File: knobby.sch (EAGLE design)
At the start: 15 parts

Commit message: Added LEDS to knobby board
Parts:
- added P1, P101: (no value), DCO_PIGGY:SPARKFUN_POTPDB12
- added S3: SWITCH-MOMENTARY-2-SMD-1101NE, SparkFun-Electromechanical:SWITCH-MOMENTARY-2-SMD-1101NE
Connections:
- net 5V: now also P1.E, P101.E
- net CLOCK_SPEED: now also P101.S
- net GND: now also S3.2
- net LOAD: now also S3.1
- net NOTE_LENGTH: now also P1.S
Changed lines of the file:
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@@
 <layer number="108" name="tplace-old" color="10" fill="1" visible="yes" active="yes"/>
 <layer number="109" name="ref-old" color="11" fill="1" visible="yes" active="yes"/>
+<layer number="110" name="fp0" color="7" fill="1" visible="yes" active="yes"/>
+<layer number="111" name="LPC17xx" color="7" fill="1" visible="yes" active="yes"/>
 <layer number="116" name="Patch_BOT" color="9" fill="4" visible="no" active="yes"/>
 <layer number="121" name="_tsilk" color="7" fill="1" visible="no" active="yes"/>
 <layer number="122" name="_bsilk" color="7" fill="1" visible="no" active="yes"/>
+<layer number="123" name="tTestmark" color="7" fill="1" visible="yes" active="yes"/>
+<layer number="124" name="bTestmark" color="7" fill="1" visible="yes" active="yes"/>
 <layer number="125" name="_tNames" color="7" fill="1" visible="no" active="yes"/>
+<layer number="131" name="tAdjust" color="7" fill="1" visible="yes" active="yes"/>
+<layer number="132" name="bAdjust" color="7" fill="1" visible="yes" active="yes"/>
 <layer number="144" name="Drill_legend" color="7" fill="1" visible="no" active="yes"/>
 <layer number="151" name="HeatSink" color="7" fill="1" visible="no" active="yes"/>
@@
 <part name="S1" library="SparkFun-Electromechanical" deviceset="SWITCH-MOMENTARY-2" device="-SMD-1101NE"/>
 <part name="S2" library="SparkFun-Electromechanical" deviceset="SWITCH-MOMENTARY-2" device="-SMD-1101NE"/>
+<part name="P101" library="DCO_PIGGY" deviceset="SPARKFUN_POT" device="PDB12"/>
+<part name="SUPPLY2" library="SparkFun-Aesthetics" deviceset="5V" device=""/>
+<part name="P1" library="DCO_PIGGY" deviceset="SPARKFUN_POT" device="PDB12"/>
+<part name="SUPPLY3" library="SparkFun-Aesthetics" deviceset="5V" device=""/>
+<part name="S3" library="SparkFun-Electromechanical" deviceset="SWITCH-MOMENTARY-2" device="-SMD-1101NE"/>
+<part name="GND2" library="SparkFun-Aesthetics" deviceset="GND" device=""/>
 </parts>
 <sheets>
@@
 <instance part="S1" gate="G$1" x="-172.72" y="96.52"/>
 <instance part="S2" gate="G$1" x="-172.72" y="96.52"/>
+<instance part="P101" gate="G$1" x="-170.18" y="83.82" rot="R270"/>
+<instance part="SUPPLY2" gate="G$1" x="-162.56" y="86.36"/>
+<instance part="P1" gate="G$1" x="-172.72" y="68.58" rot="R270"/>
+<instance part="SUPPLY3" gate="G$1" x="-165.1" y="71.12"/>
+<instance part="S3" gate="G$1" x="-175.26" y="50.8"/>
+<instance part="GND2" gate="1" x="-170.18" y="45.72"/>
 </instances>
 <busses>
@@
 <wire x1="-139.7" y1="165.1" x2="-139.7" y2="167.64" width="0.1524" layer="91"/>
 </segment>
+<segment>
+<pinref part="P101" gate="G$1" pin="E"/>
+<wire x1="-162.56" y1="83.82" x2="-162.56" y2="86.36" width="0.1524" layer="91"/>
+<pinref part="SUPPLY2" gate="G$1" pin="5V"/>
+</segment>
+<segment>
+<pinref part="P1" gate="G$1" pin="E"/>
+<pinref part="SUPPLY3" gate="G$1" pin="5V"/>
+<wire x1="-165.1" y1="68.58" x2="-165.1" y2="71.12" width="0.1524" layer="91"/>
+</segment>
 </net>
 <net name="GND" class="0">
@@
 <pinref part="GND1" gate="1" pin="GND"/>
 </segment>
+<segment>
+<pinref part="S3" gate="G$1" pin="2"/>
+<pinref part="GND2" gate="1" pin="GND"/>
+<wire x1="-170.18" y1="50.8" x2="-170.18" y2="48.26" width="0.1524" layer="91"/>
+</segment>
 </net>
 <net name="PAUSE_IN" class="0">
@@
 <pinref part="JP3" gate="G$1" pin="17"/>
 <wire x1="-148.59" y1="157.48" x2="-146.05" y2="157.48" width="0.1524" layer="91"/>
+</segment>
+<segment>
+<pinref part="S3" gate="G$1" pin="1"/>
+<wire x1="-180.34" y1="50.8" x2="-185.42" y2="50.8" width="0.1524" layer="91"/>
+<label x="-187.96" y="50.8" size="1.778" layer="95"/>
 </segment>
 </net>
@@
 <label x="-177.8" y="157.48" size="1.778" layer="95"/>
 </segment>
+<segment>
+<pinref part="P101" gate="G$1" pin="S"/>
+<wire x1="-170.18" y1="78.74" x2="-170.18" y2="76.2" width="0.1524" layer="91"/>
+<wire x1="-170.18" y1="76.2" x2="-185.42" y2="76.2" width="0.1524" layer="91"/>
+<label x="-187.96" y="76.2" size="1.778" layer="95"/>
+</segment>
 </net>
 <net name="N$29" class="0">
@@
 <label x="-147.32" y="160.02" size="1.778" layer="95"/>
 </segment>
-</net>
+<segment>
+<pinref part="P1" gate="G$1" pin="S"/>
+<wire x1="-172.72" y1="63.5" x2="-172.72" y2="60.96" width="0.1524" layer="91"/>
+<wire x1="-172.72" y1="60.96" x2="-187.96" y2="60.96" width="0.1524" layer="91"/>
+<label x="-190.5" y="60.96" size="1.778" layer="95"/>
+</segment>
+</net>

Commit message: 16 pots
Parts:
- added LED1, LED10, LED11, LED12, LED13, LED14, LED15, LED16, LED2, LED3, LED4, LED5, LED6, LED7, LED8, LED9: (no value), SparkFun-LED:LED0603
- added P10, P11, P12, P13, P14, P15, P16, P17, P2, P3, P4, P5, P6, P7, P8, P9: 10k, DCO_PIGGY:SPARKFUN_POTPDB12
- added R1, R13, R14, R15, R16, R17, R18, R19, R2, R20, R21, R22, R23, R24, R3, R4: 15k, SparkFun-Resistors:RESISTOR0603
- added S10, S11, S12, S13, S14, S15, S16, S17, S18, S19, S4, S5, S6, S7, S8, S9: SWITCH-MOMENTARY-2-SMD-1101NE, SparkFun-Electromechanical:SWITCH-MOMENTARY-2-SMD-1101NE
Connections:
- new net CHANNEL3: P5.S
- new net N$1: P2.E, R1.1
- new net N$10: P6.A, S8.2
- new net N$11: P7.E, R14.1
- new net N$12: P7.A, S9.2
- new net N$13: P8.E, R15.1
- new net N$14: P8.A, S10.2
- new net N$15: P9.E, R16.1
- new net N$16: P9.A, S11.2
- new net N$17: P10.E, R17.1
- new net N$18: P10.A, S12.2
- new net N$19: P11.E, R18.1
- new net N$2: P2.A, S4.2
- new net N$20: P11.A, S13.2
- new net N$21: P12.E, R19.1
- new net N$22: P12.A, S14.2
- new net N$23: P13.E, R20.1
- new net N$24: P13.A, S15.2
- new net N$25: P14.E, R21.1
- new net N$26: P14.A, S16.2
- new net N$27: P15.E, R22.1
- new net N$28: P15.A, S17.2
- new net N$3: P3.E, R2.1
- new net N$30: P16.E, R23.1
- new net N$31: P16.A, S18.2
- new net N$32: P17.E, R24.1
- new net N$33: P17.A, S19.2
- new net N$4: P3.A, S5.2
- new net N$5: P4.E, R3.1
- new net N$6: P4.A, S6.2
- new net N$7: P5.E, R4.1
- new net N$8: P5.A, S7.2
- new net N$9: P6.E, R13.1
- net 5V: now also R1.2, R13.2, R14.2, R15.2, R16.2, R17.2, R18.2, R19.2, R2.2, R20.2, R21.2, R22.2, R23.2, R24.2, R3.2, R4.2
- net CHANNEL0: now also P2.S
- net CHANNEL1: now also P3.S
- net CHANNEL10: now also P10.S
- net CHANNEL11: now also P11.S
- net CHANNEL12: now also P12.S
- net CHANNEL13: now also P13.S
- net CHANNEL14: now also P16.S
- net CHANNEL15: now also P17.S
- net CHANNEL2: now also P4.S
- net CHANNEL4: now also P6.S
- net CHANNEL5: now also P7.S
- net CHANNEL6: now also P14.S
- net CHANNEL7: now also P15.S
- net CHANNEL8: now also P8.S
- net CHANNEL9: now also P9.S
- net GND: now also LED1.C, LED10.C, LED11.C, LED12.C, LED13.C, LED14.C, LED15.C, LED16.C, LED2.C, LED3.C, LED4.C, LED5.C, LED6.C, LED7.C, LED8.C, LED9.C, S10.1, S11.1, S12.1, S13.1, S14.1, S15.1, S16.1, S17.1, S18.1, S19.1, S4.1, S5.1, S6.1, S7.1, S8.1, S9.1
- net LED0: now also LED16.A
- net LED1: now also LED7.A
- net LED10: now also LED11.A
- net LED11: now also LED12.A
- net LED12: now also LED13.A
- net LED13: now also LED14.A
- net LED14: now also LED15.A
- net LED15: now also LED1.A
- net LED2: now also LED6.A
- net LED3: now also LED5.A
- net LED4: now also LED4.A
- net LED5: now also LED3.A
- net LED6: now also LED2.A
- net LED7: now also LED8.A
- net LED8: now also LED9.A
- net LED9: now also LED10.A

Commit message: knobby brd
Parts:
- removed FRAME1: FRAME-LETTER, SparkFun-Aesthetics:FRAME-LETTER
- removed JP2, JP3: M20, SparkFun-Connectors:M20
- removed LED1, LED10, LED11, LED12, LED13, LED14, LED15, LED16, LED2, LED3, LED4, LED5, LED6, LED7, LED8, LED9: (no value), SparkFun-LED:LED0603
- removed P1, P101: (no value), DCO_PIGGY:SPARKFUN_POTPDB12
- removed P10, P11, P12, P13, P14, P15, P16, P17, P2, P3, P4, P5, P6, P7, P8, P9: 10k, DCO_PIGGY:SPARKFUN_POTPDB12
- removed R13, R14, R15, R16, R17, R18, R19, R2, R20, R21, R22, R23, R24, R3, R4: 15k, SparkFun-Resistors:RESISTOR0603
- removed S1, S10, S11, S12, S13, S14, S15, S16, S17, S18, S19, S2, S3, S4, S5, S6, S7, S8, S9: SWITCH-MOMENTARY-2-SMD-1101NE, SparkFun-Electromechanical:SWITCH-MOMENTARY-2-SMD-1101NE
- removed U$1: M04X2, SparkFun-Connectors:M04X2
- added CLOCK_SPEED, NOTE_LENGTH: (no value), DCO_PIGGY:SPARKFUN_POTPDB12
- added PAUSE: SWITCH-MOMENTARY-2PTH, SparkFun-Electromechanical:SWITCH-MOMENTARY-2PTH
- added POWER: (no value), SparkFun-LED:LED3MM
- added RESET: (no value), SparkFun-Electromechanical:SWITCH-SPDTPTH
- added STANDOFF1, STANDOFF2, STANDOFF3, STANDOFF4: STAND-OFF, SparkFun-Electromechanical:STAND-OFF
- added U$2: M08X2, SparkFun-Connectors:M08X2
- R1: value 15k -> (none)
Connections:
- removed net CANNEL3: JP2.4
- removed net CHANNEL0: JP2.1, P2.S
- removed net CHANNEL1: JP2.2, P3.S
- removed net CHANNEL10: JP2.11, P10.S
- removed net CHANNEL11: JP2.12, P11.S
- removed net CHANNEL12: JP2.13, P12.S
- removed net CHANNEL13: JP2.14, P13.S
- removed net CHANNEL14: JP2.15, P16.S
- removed net CHANNEL15: JP2.16, P17.S
- removed net CHANNEL2: JP2.3, P4.S
- removed net CHANNEL3: P5.S
- removed net CHANNEL4: JP2.5, P6.S
- removed net CHANNEL5: JP2.6, P7.S
- removed net CHANNEL6: JP2.7, P14.S
- removed net CHANNEL7: JP2.8, P15.S
- removed net CHANNEL8: JP2.9, P8.S
- removed net CHANNEL9: JP2.10, P9.S
- removed net LED0: JP3.1, LED16.A
- removed net LED1: JP3.2, LED7.A
- removed net LED10: JP3.11, LED11.A
- removed net LED11: JP3.12, LED12.A
- removed net LED12: JP3.13, LED13.A
- removed net LED13: JP3.14, LED14.A
- removed net LED14: JP3.15, LED15.A
- removed net LED15: JP3.16, LED1.A
- removed net LED2: JP3.3, LED6.A
- removed net LED3: JP3.4, LED5.A
- removed net LED4: JP3.5, LED4.A
- removed net LED5: JP3.6, LED3.A
- removed net LED6: JP3.7, LED2.A
- removed net LED7: JP3.8, LED8.A
- removed net LED8: JP3.9, LED9.A
- removed net LED9: JP3.10, LED10.A
- removed net N$10: P6.A, S8.2
- removed net N$11: P7.E, R14.1
- removed net N$12: P7.A, S9.2
- removed net N$13: P8.E, R15.1
- removed net N$14: P8.A, S10.2
- removed net N$15: P9.E, R16.1
- removed net N$17: P10.E, R17.1
- removed net N$18: P10.A, S12.2
- removed net N$19: P11.E, R18.1
- removed net N$2: P2.A, S4.2
- removed net N$20: P11.A, S13.2
- removed net N$21: P12.E, R19.1
- removed net N$22: P12.A, S14.2
- removed net N$23: P13.E, R20.1
- removed net N$24: P13.A, S15.2
- removed net N$25: P14.E, R21.1
- removed net N$26: P14.A, S16.2
- removed net N$27: P15.E, R22.1
- removed net N$28: P15.A, S17.2
- removed net N$29: JP3.19
- removed net N$3: P3.E, R2.1
- removed net N$30: P16.E, R23.1
- removed net N$31: P16.A, S18.2
- removed net N$32: P17.E, R24.1
- removed net N$33: P17.A, S19.2
- removed net N$4: P3.A, S5.2
- removed net N$5: P4.E, R3.1
- removed net N$6: P4.A, S6.2
- removed net N$7: P5.E, R4.1
- removed net N$8: P5.A, S7.2
- removed net N$9: P6.E, R13.1
- net 5V: now also CLOCK_SPEED.E, NOTE_LENGTH.E, U$2.1; no longer JP3.20, P1.E, P101.E, R13.2, R14.2, R15.2, R16.2, R17.2, R18.2, R19.2, R2.2, R20.2, R21.2, R22.2, R23.2, R24.2, R3.2, R4.2
- net CLOCK_SPEED: now also CLOCK_SPEED.S, U$2.7; no longer JP2.17, P101.S
- net GND: now also POWER.C, RESET.S, U$2.16; no longer JP2.20, LED1.C, LED10.C, LED11.C, LED12.C, LED13.C, LED14.C, LED15.C, LED16.C, LED2.C, LED3.C, LED4.C, LED5.C, LED6.C, LED7.C, LED8.C, LED9.C, S10.1, S11.1, S12.1, S13.1, S14.1, S15.1, S16.1, S17.1, S18.1, S19.1, S3.2, S4.1, S5.1, S6.1, S7.1, S8.1, S9.1
- net LOAD: now also RESET.P, U$2.11; no longer JP3.17, S3.1
- net LOAD0: now also U$2.6; no longer U$1.2
- net LOAD1: now also U$2.8; no longer U$1.4
- net LOAD2: now also U$2.10; no longer U$1.6
- net LOAD3: now also U$2.12; no longer U$1.8
- net N$1: now also POWER.A; no longer P2.E
- net N$16: now also U$2.14; no longer P9.A, S11.2
- net NOTE_LENGTH: now also NOTE_LENGTH.S, U$2.9; no longer JP3.18, P1.S
- net PAUSE_IN: now also PAUSE.1, U$2.3; no longer JP2.18, S1.1, S2.1
- net PAUSE_OUT: now also PAUSE.2, U$2.5; no longer JP2.19, S1.2, S2.2
- net RESET0: now also U$2.13; no longer U$1.1
- net RESET1: now also U$2.15; no longer U$1.3
- net RESET2: now also U$2.2; no longer U$1.5
- net RESET3: now also U$2.4; no longer U$1.7
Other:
- moved on the sheet: R1, R10, R11, R12, R5, R6, R7, R8, R9, SW1

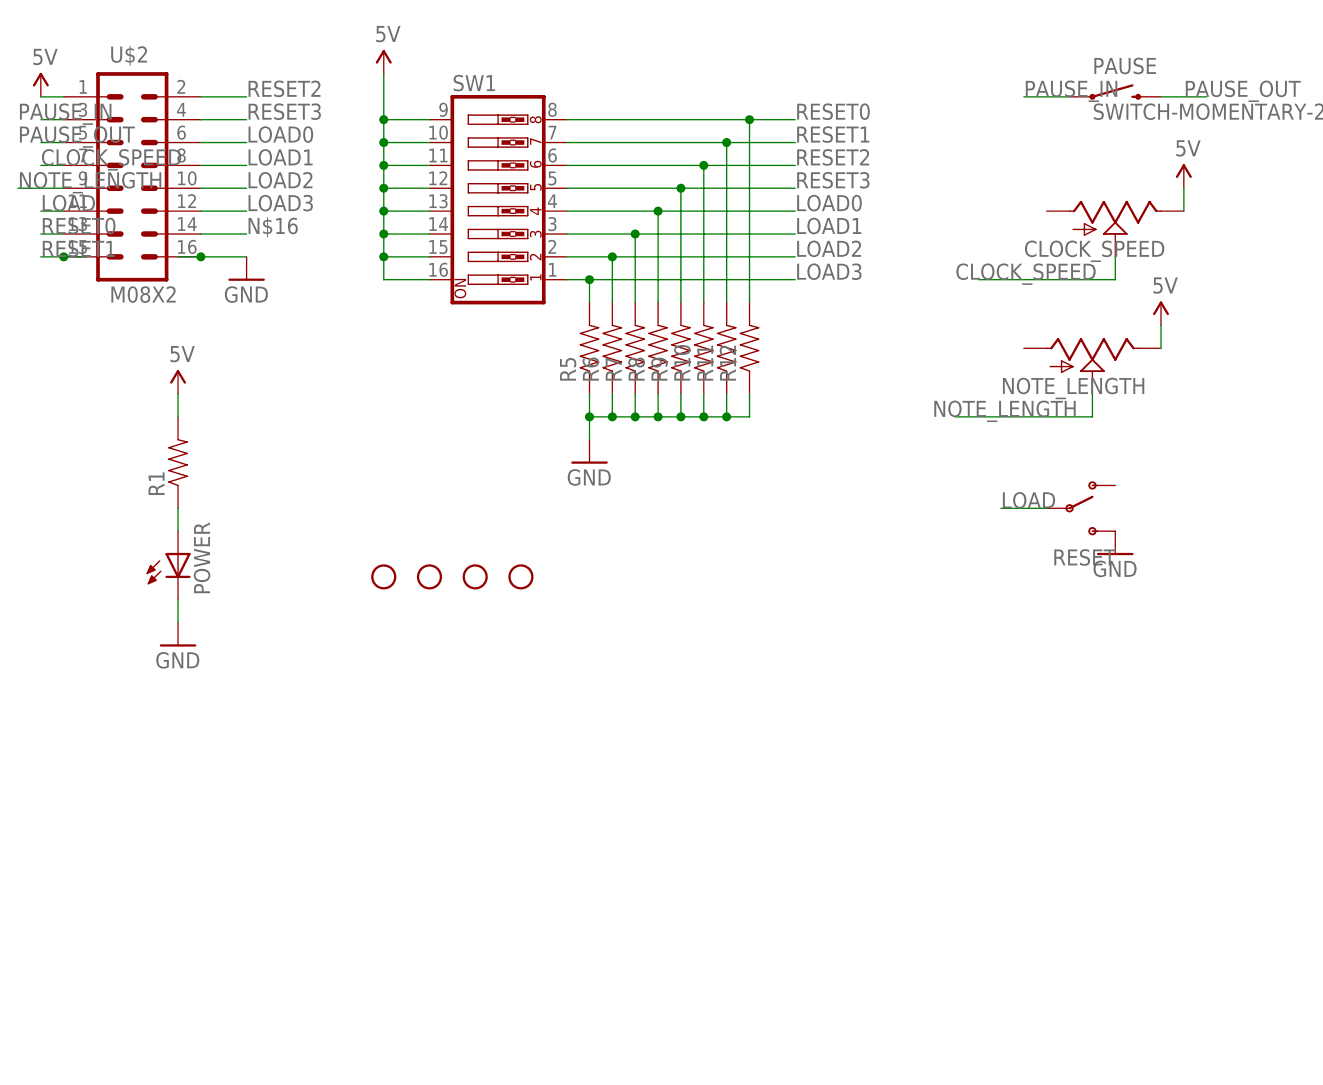
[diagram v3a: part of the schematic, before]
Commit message: Knobby board layed out with 4 jacks
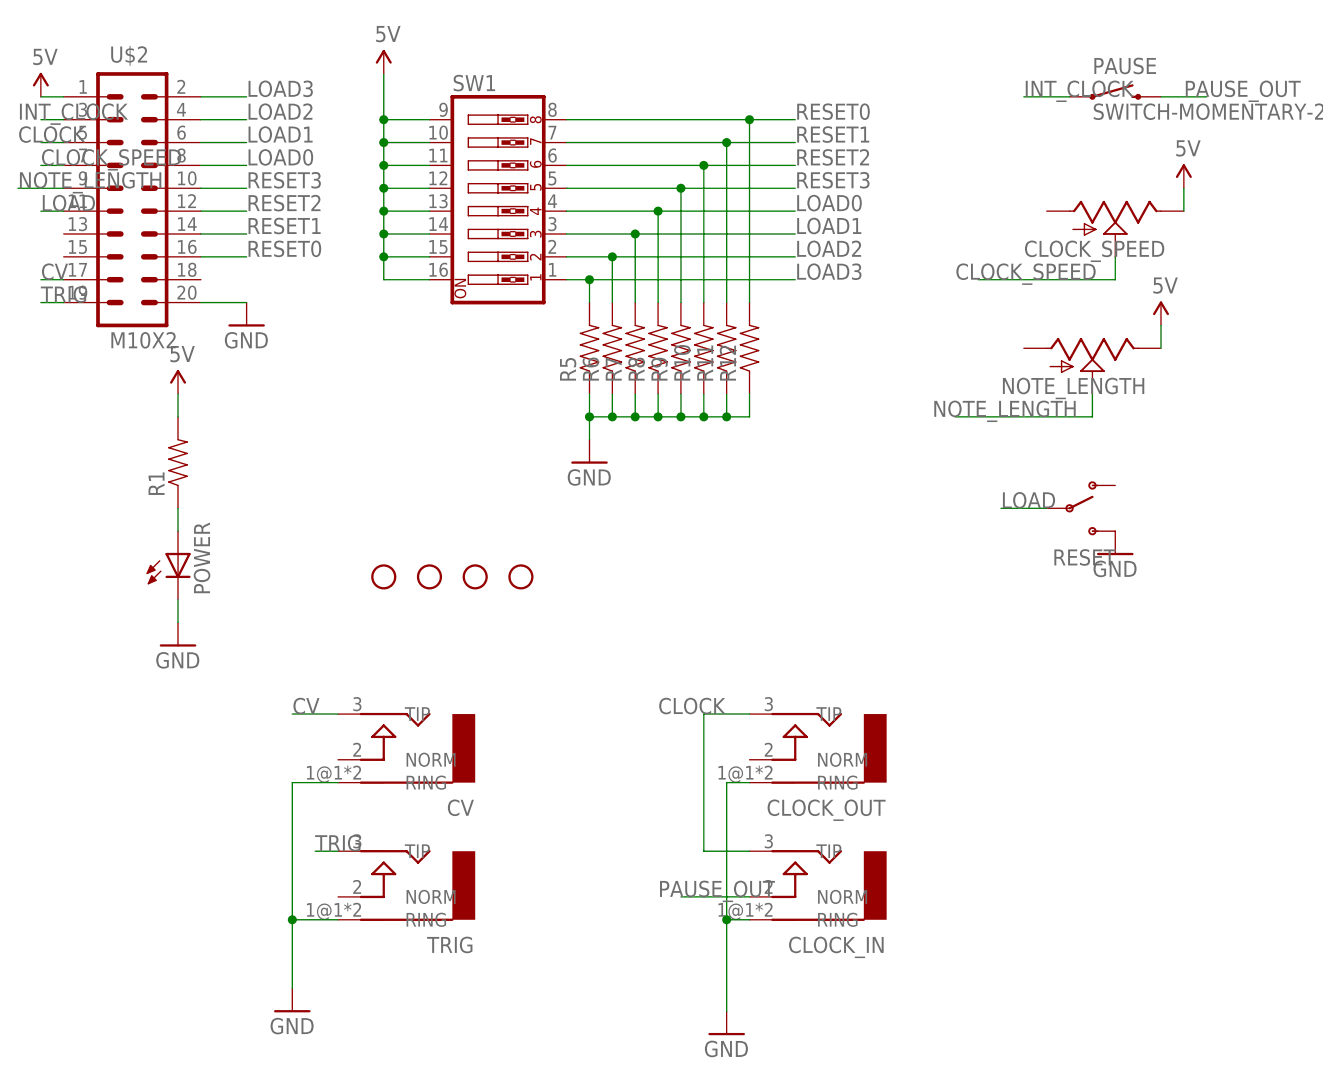
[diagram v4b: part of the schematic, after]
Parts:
- added CLOCK_IN, CLOCK_OUT, CV, TRIG: AUDIO-JACKERTHENVAR, erthenvar:AUDIO-JACKERTHENVAR
- U$2: value M08X2 -> M10X2; device SparkFun-Connectors:M08X2 -> SparkFun-Connectors:M10X2
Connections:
- net PAUSE_IN renamed INT_CLOCK
- removed net N$16: U$2.14
- new net CLOCK: CLOCK_IN.TIP, CLOCK_OUT.TIP, U$2.5
- new net CV: CV.TIP, U$2.17
- new net TRIG: TRIG.TIP, U$2.19
- net GND: now also CLOCK_IN.RING, CLOCK_OUT.RING, CV.RING, TRIG.RING, U$2.20; no longer U$2.16
- net LOAD0: now also U$2.8; no longer U$2.6
- net LOAD1: now also U$2.6; no longer U$2.8
- net LOAD2: now also U$2.4; no longer U$2.10
- net LOAD3: now also U$2.2; no longer U$2.12
- net PAUSE_OUT: now also CLOCK_IN.NORM; no longer U$2.5
- net RESET0: now also U$2.16; no longer U$2.13
- net RESET1: now also U$2.14; no longer U$2.15
- net RESET2: now also U$2.12; no longer U$2.2
- net RESET3: now also U$2.10; no longer U$2.4
